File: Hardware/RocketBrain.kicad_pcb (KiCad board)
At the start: 2 copper layers, 22 x 52 mm, 46 parts, among them J1 Screw_Terminal_01x02, J2 1x3 picoblade, J3 1x3 picoblade, J4 1x2 picoblade, J5 DM3CS-SF, J6 Screw_Terminal_01x02, Q1 G1003A, U1 Pico, U2 LSM9DS1, U3 MPU-6050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

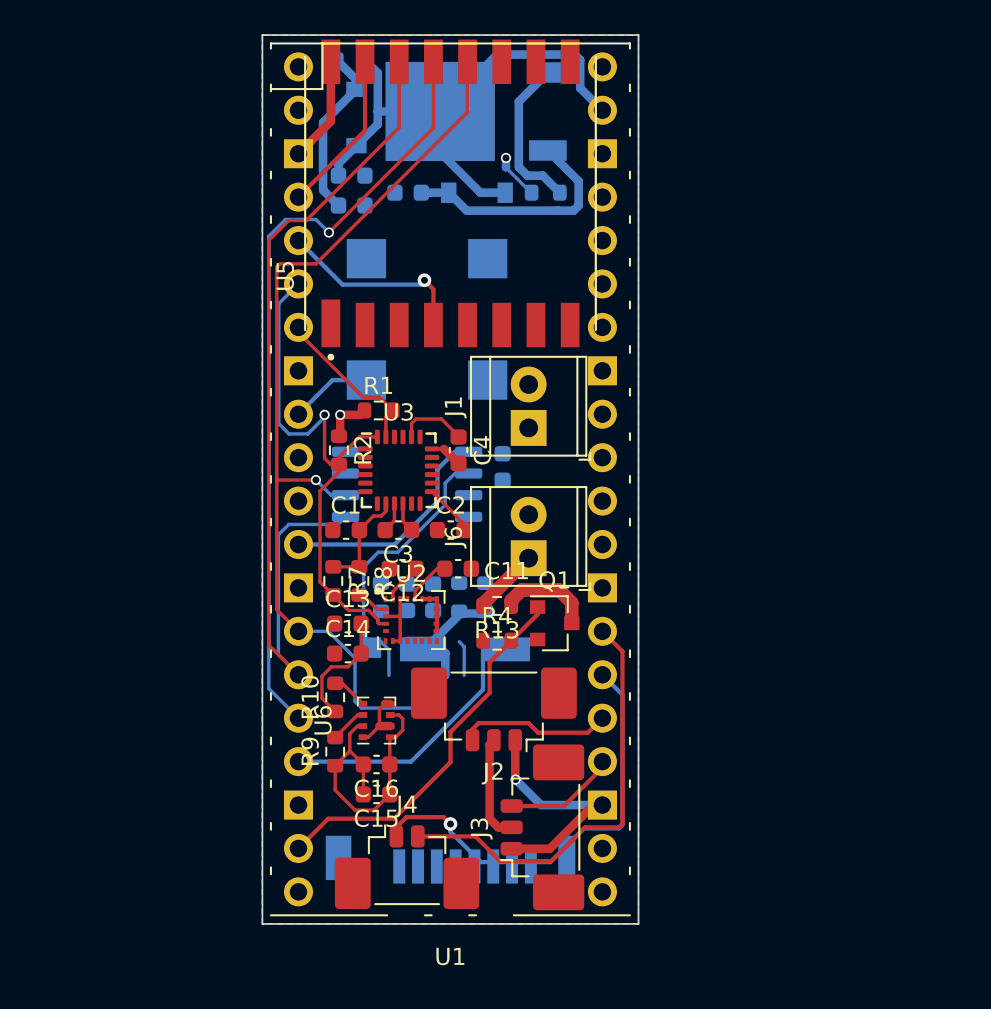
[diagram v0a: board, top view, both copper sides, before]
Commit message: Add 2nd pyro, smd headers
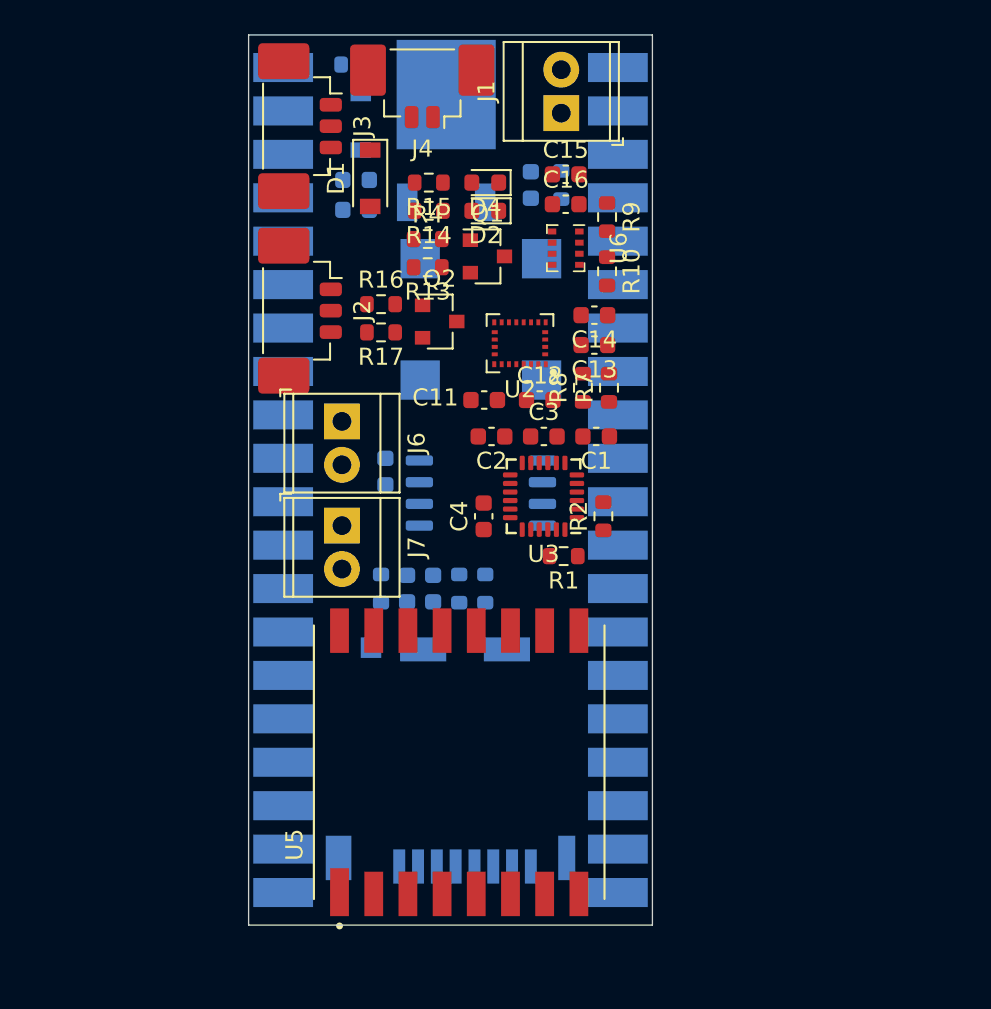
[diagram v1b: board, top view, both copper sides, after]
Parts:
- added D2: LED red, LED_SMD:LED_0603_1608Metric, F.Cu at (138.8, 65.5)
- added D4: LED, LED_SMD:LED_0603_1608Metric, F.Cu at (138.8, 63.9)
- added J7: Screw_Terminal_01x02, TerminalBlock_TE-Connectivity:TerminalBlock_TE_282834-2_1x02_P2.54mm_Horizontal, F.Cu at (130.4, 83.9)
- added Q2: G1003A, Package_TO_SOT_SMD:SOT-23, F.Cu at (136.1, 72.0)
- added R14: 220, Resistor_SMD:R_0603_1608Metric, F.Cu at (135.5, 65.5)
- added R15: 220, Resistor_SMD:R_0603_1608Metric, F.Cu at (135.5, 63.9)
- added R16: 1k, Resistor_SMD:R_0603_1608Metric, F.Cu at (132.7, 71.0)
- added R17: 10, Resistor_SMD:R_0603_1608Metric, F.Cu at (132.7, 72.6)
- D1: moved to F.Cu
- U1: footprint RocketBrain:RPi_Pico_HAT -> RocketBrain:RPi_Pico_HAT_smd; moved to B.Cu
- moved J4 44.6 mm to (135.1, 58.8), turned to 180 degrees
- moved J3 43.1 mm to (128.5, 60.6), turned to 270 degrees
- moved C15 37.9 mm to (143.5, 63.4), turned to 0 degrees
- moved R9 35.1 mm to (145.9, 65.9), turned to 270 degrees
- moved C16 34.6 mm to (143.5, 65.1), turned to 0 degrees
- moved U5 33.3 mm to (137.3, 97.8)
- moved U6 29.8 mm to (143.5, 67.7), turned to 270 degrees
- moved R10 29.6 mm to (145.9, 69.1), turned to 270 degrees
- moved J2 26.2 mm to (128.5, 71.4), turned to 270 degrees
- moved C14 24.5 mm to (145.2, 71.6), turned to 180 degrees
- moved R4 23.8 mm to (135.4, 67.2)
- moved Q1 21.8 mm to (138.9, 68.2)
- moved C13 21.8 mm to (145.2, 73.4), turned to 180 degrees
- moved R13 20.2 mm to (135.4, 68.8)
- moved R7 19.7 mm to (146.0, 75.9), turned to 90 degrees
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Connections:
- C15 pad 2: +3V3 -> GND
- C16 pad 2: +3V3 -> GND
- Q1 pad 1: /Pyro/pyro -> /Pyro/pyro1
- R4 pad 2: /Pyro/pyro -> /Pyro/pyro1
- U1 pad 10: Net-(U1-Pad10) -> /RPi Pico & Motors/boot
- U1 pad 19: /Pyro/pyro -> /RPi Pico & Motors/pyro
- U1 pad 29: Net-(U1-Pad29) -> /RPi Pico & Motors/buzz
- U1 pad 9: /RPi Pico & Motors/buzz -> /RPi Pico & Motors/ready
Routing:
- net MISO: track 62.2 -> 0.00 mm, vias 1 -> 0
- net CLK: track 56.5 -> 0.00 mm, vias 1 -> 0
- net MOSI: track 55.5 -> 0.00 mm
- net +3V3: track 47.9 -> 0.00 mm, vias 1 -> 0
- net +5V: track 38.2 -> 0.00 mm
- net /RPi Pico & Motors/SDA: track 33.3 -> 0.00 mm, vias 1 -> 0
- net GND: track 33.2 -> 0.00 mm, vias 2 -> 0
- net /RPi Pico & Motors/rw+: track 25.5 -> 0.00 mm, vias 1 -> 0
- net /RPi Pico & Motors/rw-: track 25.2 -> 0.00 mm
- net /Pyro/pyro: track 22.2 -> 0.00 mm
- net /Data Logging/~CS_SD: track 15.4 -> 0.00 mm
- net +BATT: track 13.7 -> 0.00 mm
- net /RPi Pico & Motors/SCL: track 13.4 -> 0.00 mm
- net /Data Logging/~CS_flash: track 13.3 -> 0.00 mm
- net /RPi Pico & Motors/~RESET_LoRa: track 11.4 -> 0.00 mm, vias 1 -> 0
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- removed copper zone on B.Cu, net GND
- removed copper zone on F.Cu, net GND
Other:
- board size 22 x 52 mm -> 23.6 x 52.1 mm

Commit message: Update schematic, component placement
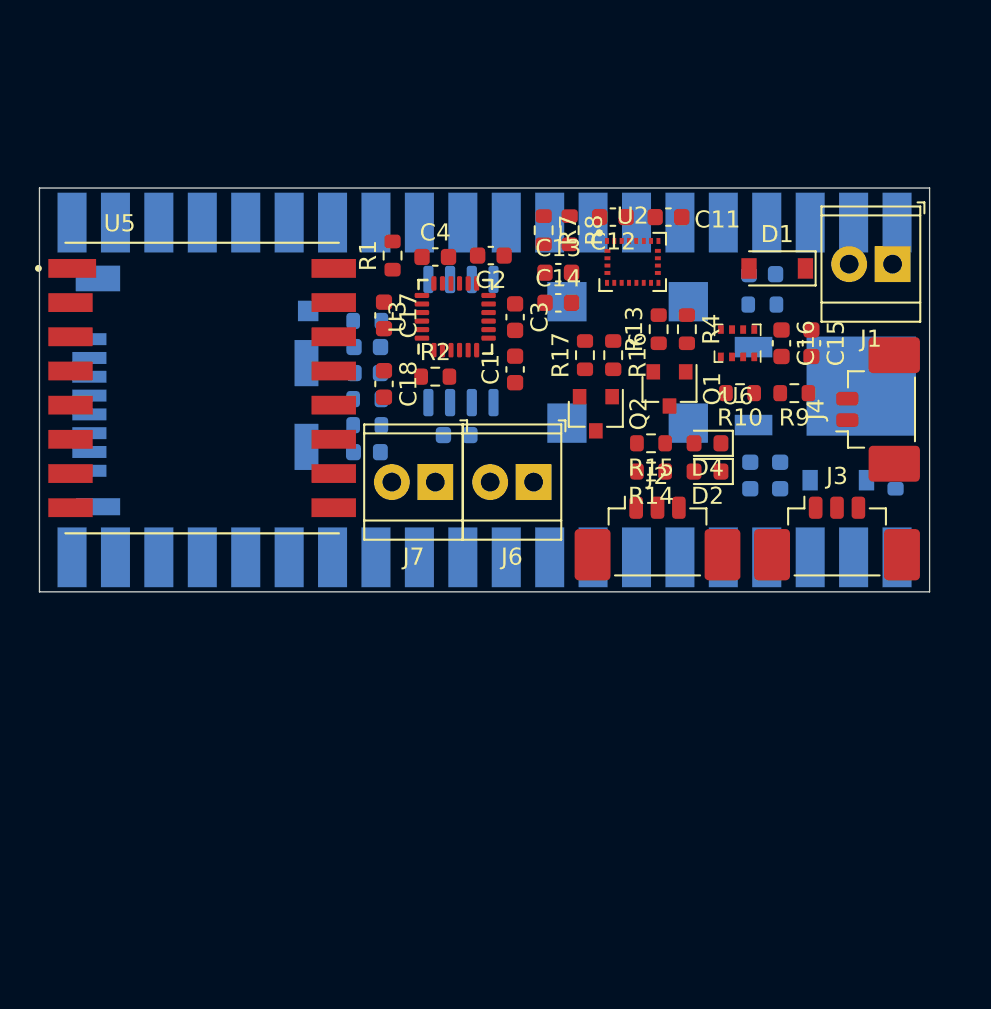
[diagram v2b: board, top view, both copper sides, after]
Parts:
- added C17: 22u, Capacitor_SMD:C_0603_1608Metric, F.Cu at (132.9, 71.7)
- added C18: 0.1u, Capacitor_SMD:C_0603_1608Metric, F.Cu at (132.9, 75.7)
- added L1: 470n, Inductor_SMD:L_0603_1608Metric, B.Cu at (131.9, 79.7)
- D4: value LED -> LED green
- moved R5 39.7 mm to (162.8, 81.0), turned to 90 degrees
- moved J3 38.8 mm to (159.4, 84.2), turned to 0 degrees
- moved D3 34.9 mm to (159.4, 81.3), turned to 0 degrees
- moved J4 31.9 mm to (161.2, 77.2), turned to 90 degrees
- moved C9 30.2 mm to (156.0, 81.0), turned to 270 degrees
- moved C7 27.8 mm to (154.3, 81.0), turned to 270 degrees
- moved J5 27.1 mm to (121.2, 76.0), turned to 90 degrees
- moved U4 26.8 mm to (158.7, 75.8), turned to 0 degrees
- moved U5 26.6 mm to (122.2, 75.9), turned to 0 degrees
- moved D1 24.4 mm to (155.9, 68.9), turned to 180 degrees
- moved J2 24.0 mm to (148.9, 84.2), turned to 0 degrees
- moved J1 21.3 mm to (162.6, 68.7), turned to 180 degrees
- moved R1 20.2 mm to (133.4, 68.2), turned to 90 degrees
- moved D2 20.0 mm to (151.8, 80.8)
- moved D4 20.0 mm to (151.8, 79.1)
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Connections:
- C6 pad 1: +3V3 -> Net-(C6-Pad1)
- C8 pad 1: +3V3 -> Net-(C6-Pad1)
- J5 pad 4: +3V3 -> Net-(C6-Pad1)
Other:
- board size 23.6 x 52.1 mm -> 52.1 x 23.6 mm

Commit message: Update component placement
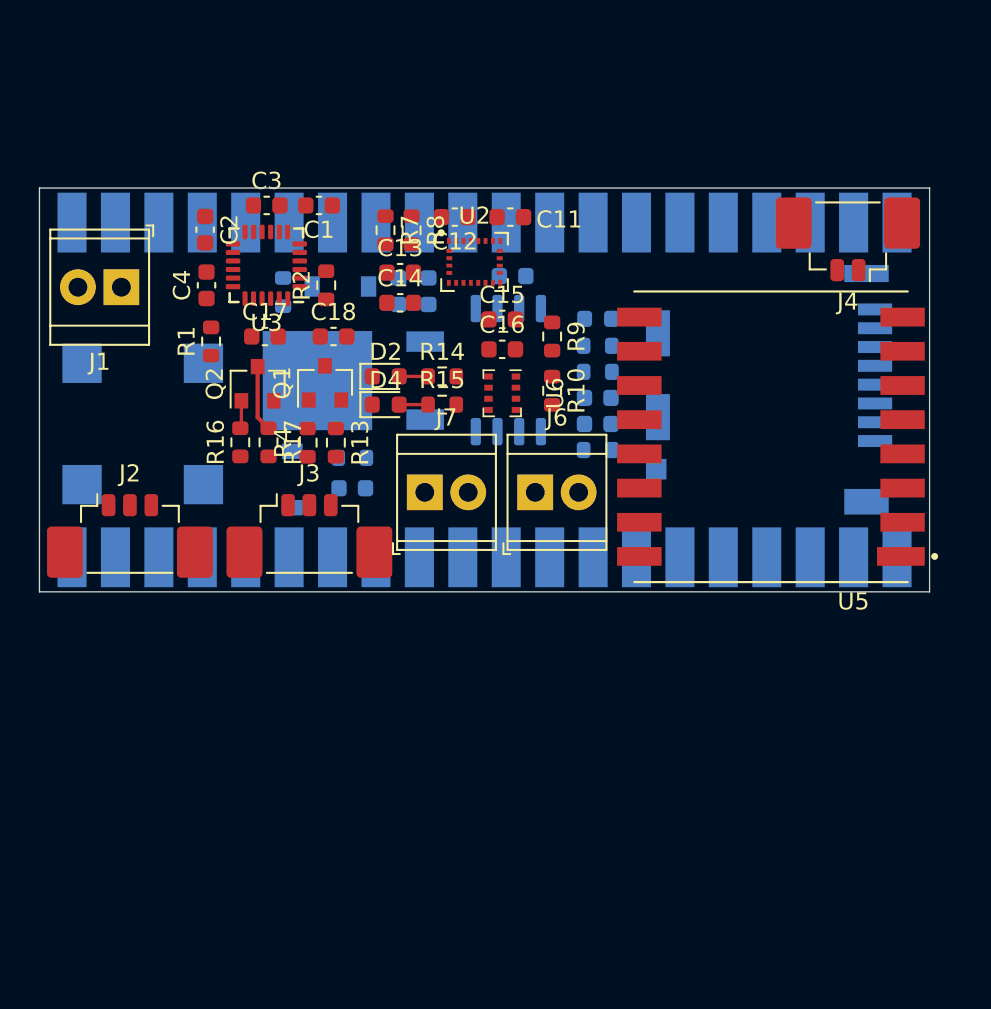
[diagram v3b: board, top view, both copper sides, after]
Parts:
- D1: moved to B.Cu
- moved J1 45.1 mm to (117.5, 70.0)
- moved R5 37.4 mm to (127.0, 70.3), turned to 270 degrees
- moved J5 34.8 mm to (156.0, 76.0), turned to 270 degrees
- moved U5 33.4 mm to (155.5, 78.8), turned to 180 degrees
- moved D3 31.3 mm to (130.3, 70.0), turned to 180 degrees
- moved D1 30.9 mm to (127.5, 81.2), turned to 270 degrees
- moved J2 30.9 mm to (118.0, 84.0)
- moved J3 30.9 mm to (128.5, 84.0)
- moved LS1 28.6 mm to (118.8, 78.0), turned to 90 degrees
- moved U4 27.6 mm to (131.1, 75.5), turned to 180 degrees
- moved C5 27.1 mm to (131.0, 81.8), turned to 0 degrees
- moved R3 25.6 mm to (131.0, 80.0), turned to 0 degrees
- moved C9 24.8 mm to (133.7, 70.2), turned to 90 degrees
- moved R4 23.2 mm to (128.4, 79.1), turned to 90 degrees
- moved R16 22.4 mm to (124.5, 79.1), turned to 90 degrees
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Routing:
- net Net-(Q2-Pad3): track 0.00 -> 3.87 mm
- net Net-(D4-Pad2): track 0.00 -> 1.69 mm
- net Net-(D2-Pad2): track 0.00 -> 1.69 mm
- net /Pyro/pyro2: track 0.00 -> 1.63 mm

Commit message: Update schematic and routing
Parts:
- moved J2 35.9 mm to (150.0, 67.8), turned to 180 degrees
- moved L1 3.15 mm to (145.4, 75.0)
- moved R11 2.95 mm to (145.4, 72.0)
- moved J3 1.27 mm to (127.2, 84.2)
- moved C10 0.35 mm to (140.4, 69.0)
- moved C7 0.25 mm to (135.5, 70.0)
- moved C9 0.25 mm to (133.7, 70.0)
- moved U4 0.22 mm to (131.0, 75.2), turned to 0 degrees
- moved R6 0.07 mm to (145.4, 73.5)
- turned R2 to 270 degrees
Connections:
- net /RPi Pico & Motors/pyro renamed Net-(U1-Pad19)
- U1 pad 1: Net-(U1-Pad1) -> /RPi Pico & Motors/ready
- U1 pad 11: /RPi Pico & Motors/INT_6050 -> Net-(U1-Pad11)
- U1 pad 2: Net-(U1-Pad2) -> /RPi Pico & Motors/INT_6050
- U1 pad 20: Net-(U1-Pad20) -> /RPi Pico & Motors/~CS_LoRa
- U1 pad 32: Net-(U1-Pad32) -> /Pyro/pyro2
- U1 pad 34: Net-(U1-Pad34) -> /Pyro/pyro1
- U1 pad 4: /RPi Pico & Motors/~CS_LoRa -> Net-(U1-Pad4)
- U1 pad 9: /RPi Pico & Motors/ready -> Net-(U1-Pad9)
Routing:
- net GND: track 0.00 -> 136.4 mm, vias 0 -> 19
- net +3V3: track 0.00 -> 115.6 mm, vias 0 -> 13
- net +5V: track 0.00 -> 90.7 mm, vias 0 -> 4
- net /RPi Pico & Motors/~RESET_LoRa: track 0.00 -> 51.0 mm, vias 0 -> 2
- net +BATT: track 0.00 -> 49.7 mm
- net MOSI: track 0.00 -> 48.7 mm, vias 0 -> 2
- net CLK: track 0.00 -> 42.6 mm, vias 0 -> 3
- net MISO: track 0.00 -> 35.7 mm, vias 0 -> 3
- net /RPi Pico & Motors/TVC_y: track 0.00 -> 34.1 mm, vias 0 -> 2
- net /RPi Pico & Motors/ready: track 0.00 -> 33.2 mm, vias 0 -> 2
- net /Data Logging/~CS_SD: track 0.00 -> 31.4 mm, vias 0 -> 2
- net /RPi Pico & Motors/buzz: track 0.00 -> 27.8 mm, vias 0 -> 2
- net /RPi Pico & Motors/SDA: track 0.00 -> 27.4 mm
- net /RPi Pico & Motors/~CS_LoRa: track 0.00 -> 26.4 mm, vias 0 -> 1
- net /RPi Pico & Motors/rw-: track 0.00 -> 22.2 mm, vias 0 -> 1
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- added copper zone on In1.Cu, net +3V3
- added copper zone on In2.Cu, net GND
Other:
- board size 52.1 x 23.6 mm -> 52 x 24 mm
- copper layers 2 -> 4
- net class power: trace_width 0.5 -> 0.4
- net class pyro: trace_width 0.8 -> 0.6

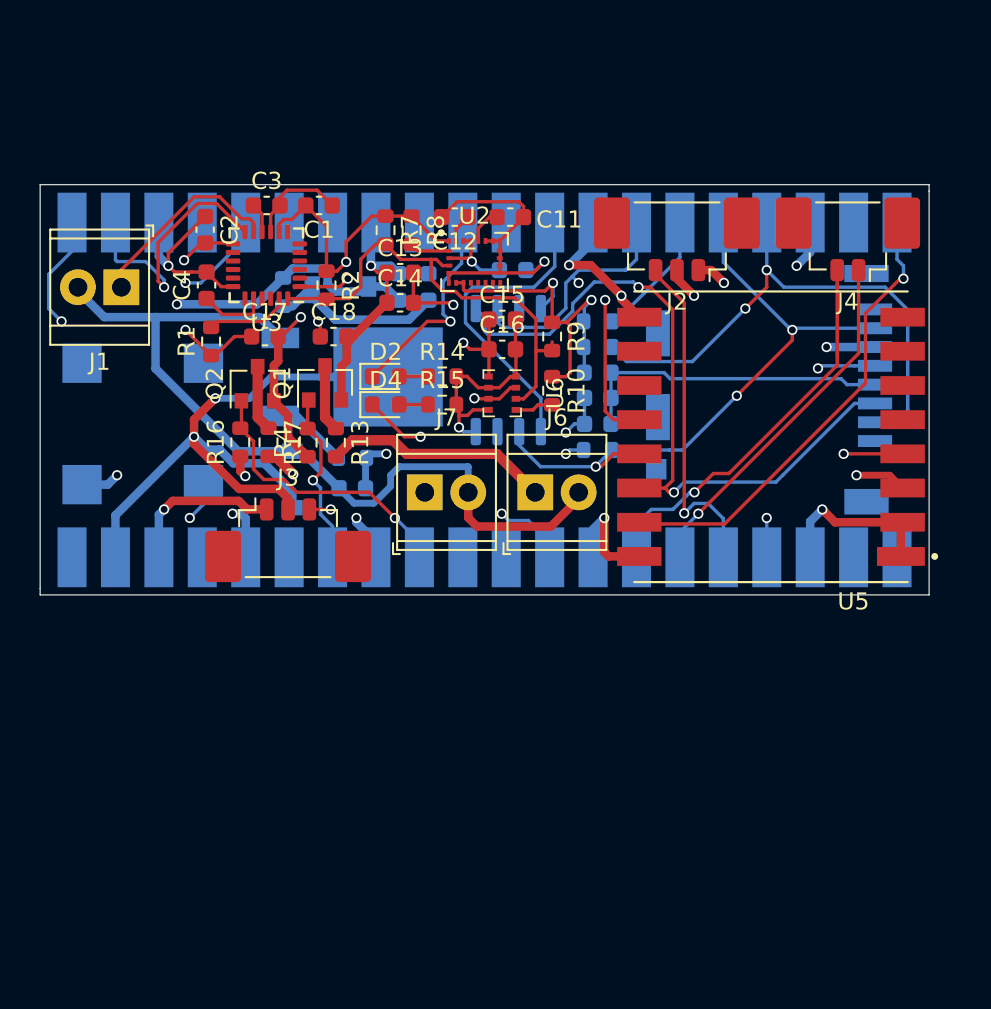
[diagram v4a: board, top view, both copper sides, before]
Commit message: Modify RPi Pico footprint, update routing
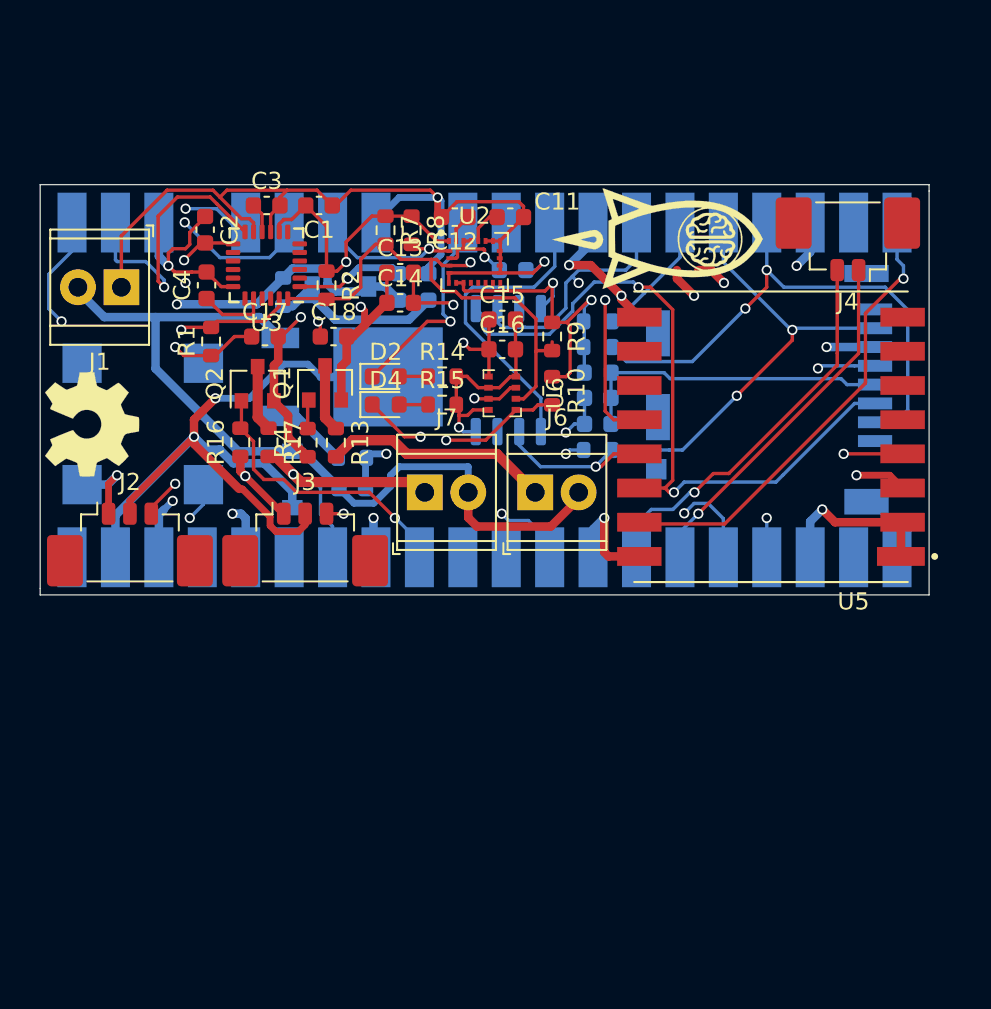
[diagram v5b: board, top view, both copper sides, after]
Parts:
- added G***: LOGO, RocketBrain:oshw_logo, F.Cu at (115.8, 78.0)
- added G***: LOGO, RocketBrain:RB_logo, F.Cu at (149.0, 67.5)
- U1: footprint RocketBrain:RPi_Pico_HAT_smd -> RocketBrain:RPi_Pico_HAT_smd_mod
- moved J2 36.1 mm to (118.0, 84.5), turned to 0 degrees
- moved J3 1.03 mm to (128.2, 84.5)
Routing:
- net /RPi Pico & Motors/SCL: track 9.56 -> 63.5 mm, vias 0 -> 3
- net GND: track 136.4 -> 163.8 mm, vias 19 -> 20
- net /RPi Pico & Motors/SDA: track 27.4 -> 54.2 mm, vias 0 -> 2
- net /RPi Pico & Motors/TVC_x: track 19.2 -> 40.5 mm, vias 1 -> 2
- net +5V: track 90.7 -> 99.6 mm
- net /RPi Pico & Motors/~RESET_LoRa: track 51.0 -> 57.4 mm, vias 2 -> 3
- net /Pyro/pyro1: track 9.32 -> 5.78 mm, vias 1 -> 0
- net /RPi Pico & Motors/INT_6050: track 14.5 -> 15.7 mm
- net /RPi Pico & Motors/TVC_y: track 34.1 -> 33.3 mm

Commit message: Update silkscreen
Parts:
- removed the G*** at (115.8, 78.0)
- LS1: footprint RocketBrain:MLT8530 -> MLT8530
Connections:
- U1 pad 31: Net-(U1-Pad31) -> /Pyro/pyro1
- U1 pad 34: /Pyro/pyro1 -> Net-(U1-Pad34)
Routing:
- net /Pyro/pyro1: track 5.78 -> 19.1 mm, vias 0 -> 1
- net Net-(U1-Pad34): track 0.00 -> 4.08 mm
- net GND: track 163.8 -> 165.8 mm

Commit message: Update silkscreen
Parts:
- added G***: LOGO, RocketBrain:oshw_logo, F.Cu at (118.2, 77.0)
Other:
- board text added: "+"
- board text added: "Batt"
- board text added: "RocketBrain v1.0.0"
- board text added: "TVC x"
- board text added: "TVC y"
- board text added: "pyro 1"
- board text added: "pyro 2"
